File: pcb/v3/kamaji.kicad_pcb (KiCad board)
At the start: 2 copper layers, 100 x 100 mm, 41 parts, among them J1 UART, J10 USB_A, J2 ICSP, J3 RJ10, J4 RJ10, J5 RJ10, J6 RJ10, J7 RJ10, J8 RJ10, J9 USB_B, Q1 2N3904, Q2 IRL540N, SW1 SW_Push, SW2 SW_Push, SW3 SW_Push, U1 ATMEGA644P-20PU, U2 BOOST_24V, Y1 20MHz

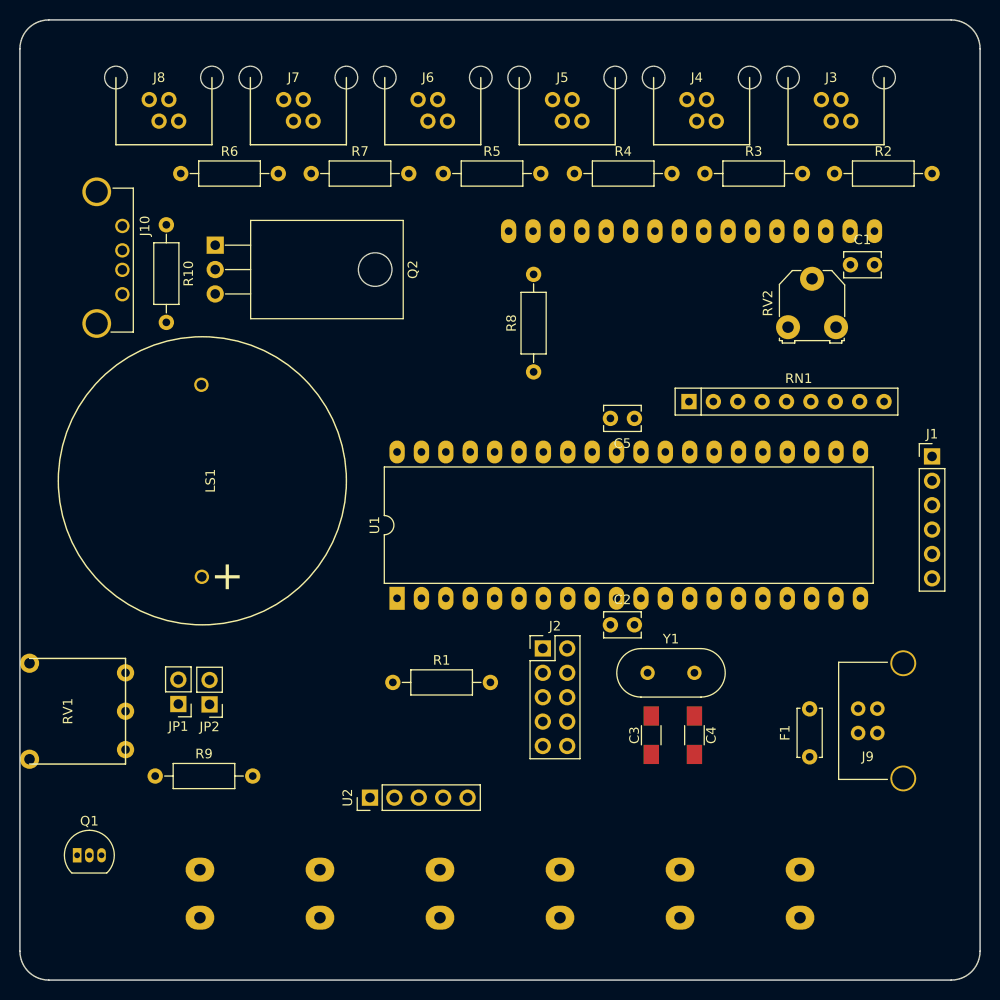
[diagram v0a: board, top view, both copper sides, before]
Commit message: mostly finish the v3 layout
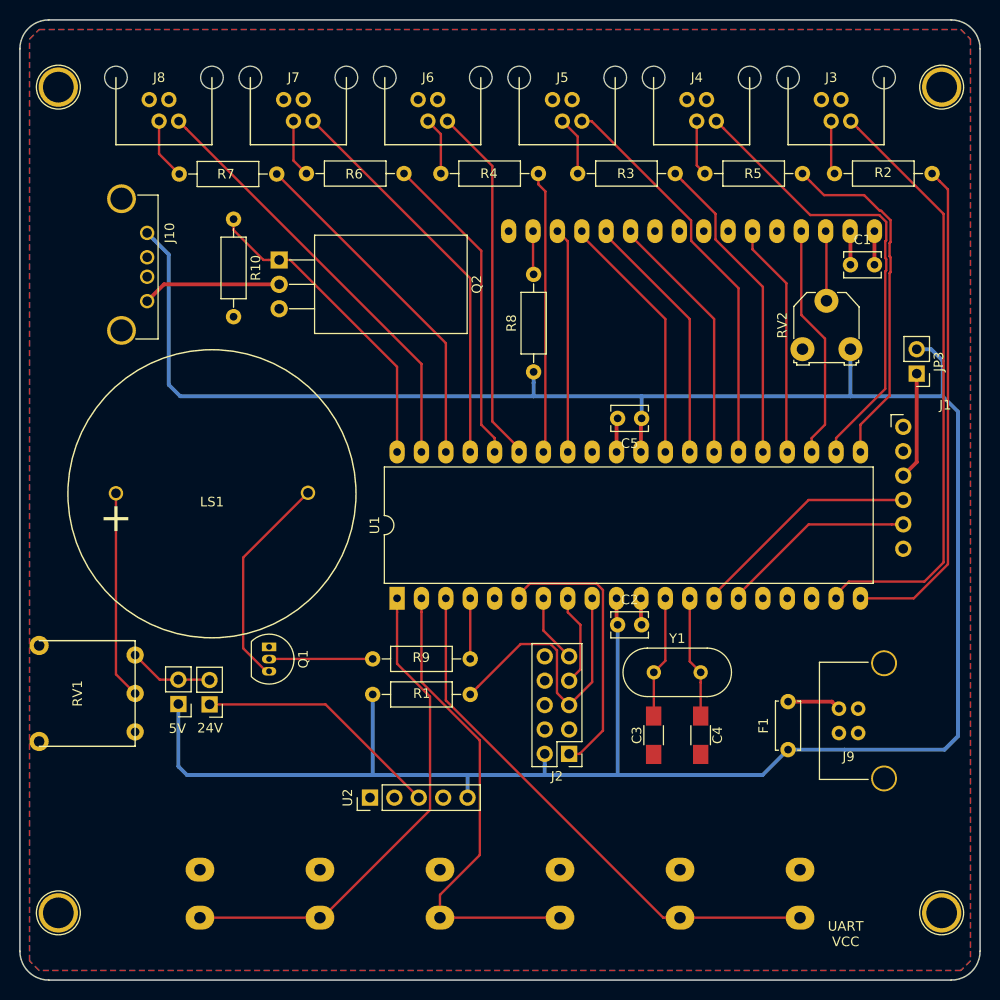
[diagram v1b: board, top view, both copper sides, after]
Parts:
- removed RN1: 10K, Resistors_THT:R_Array_SIP9
- added JP3: UART_PWR, Pin_Headers:Pin_Header_Straight_1x02_Pitch2.54mm, F.Cu at (143.4, 86.8)
- added REF**: 1pin, Connectors:1pin, F.Cu at (146.0, 143.0)
- added REF**: 1pin, Connectors:1pin, F.Cu at (54.0, 143.0)
- added REF**: 1pin, Connectors:1pin, F.Cu at (54.0, 57.0)
- added REF**: 1pin, Connectors:1pin, F.Cu at (146.0, 57.0)
- J1: value UART -> UART_6pin; footprint Pin_Headers:Pin_Header_Straight_1x06_Pitch2.54mm -> kamaji:Pin_Header_Angled_1x06_Pitch2.54mm
- Q2: footprint TO_SOT_Packages_THT:TO-220-3_Horizontal -> kamaji:TO-220-3_Horizontal
- moved Q1 29.5 mm to (76.0, 115.3), turned to 270 degrees
- moved R5 27.2 mm to (121.3, 66.0)
- moved R9 25.7 mm to (86.7, 116.5)
- moved R4 13.9 mm to (93.8, 66.0)
- moved R7 13.8 mm to (66.6, 66.0)
- moved R3 13.2 mm to (108.1, 66.0)
- moved R6 13.1 mm to (79.8, 66.0)
- moved J2 11.3 mm to (107.2, 126.4), turned to 180 degrees
- moved R10 7.02 mm to (72.2, 70.8)
- moved Q2 6.84 mm to (77.0, 75.0)
- moved J1 4.30 mm to (142.0, 92.4)
- moved RV2 2.74 mm to (131.5, 84.3)
- moved J10 2.68 mm to (63.2, 72.2)
- moved R1 2.44 mm to (86.7, 120.2)
- moved F1 2.37 mm to (130.0, 126.0)
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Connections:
- net /MC_RX renamed /AVR_RX
- net /MC_TX renamed /AVR_TX
- DS1 pad 11: Net-(DS1-Pad11) -> /LCD_D4
- DS1 pad 12: Net-(DS1-Pad12) -> /LCD_D5
- DS1 pad 13: Net-(DS1-Pad13) -> /LCD_D6
- DS1 pad 14: Net-(DS1-Pad14) -> /LCD_D7
- DS1 pad 4: Net-(DS1-Pad4) -> /LCD_RS
- DS1 pad 6: Net-(DS1-Pad6) -> /LCD_EN
- J1 pad 3: VCC -> Net-(J1-Pad3)
- J3 pad 2: /LED1 -> Net-(J3-Pad2)
- J4 pad 2: /LED2 -> Net-(J4-Pad2)
- J5 pad 2: /LED3 -> Net-(J5-Pad2)
- J6 pad 2: /LED4 -> Net-(J6-Pad2)
- J7 pad 2: /LED5 -> Net-(J7-Pad2)
- J8 pad 2: /LED6 -> Net-(J8-Pad2)
- R2 pad 1: /LED1 -> Net-(J3-Pad2)
- R2 pad 2: Net-(R2-Pad2) -> /LED1
- R3 pad 1: /LED2 -> Net-(J5-Pad2)
- R3 pad 2: Net-(R3-Pad2) -> /LED3
- R4 pad 1: /LED3 -> Net-(J6-Pad2)
- R4 pad 2: Net-(R4-Pad2) -> /LED4
- R5 pad 1: /LED4 -> Net-(J4-Pad2)
- R5 pad 2: Net-(R5-Pad2) -> /LED2
- R6 pad 1: /LED6 -> Net-(J7-Pad2)
- R6 pad 2: Net-(R6-Pad2) -> /LED5
- R7 pad 1: /LED5 -> Net-(J8-Pad2)
- R7 pad 2: Net-(R7-Pad2) -> /LED6
- U1 pad 1: /CBTN1 -> /CBTN3
- U1 pad 16: Net-(R2-Pad2) -> (no net)
- U1 pad 17: Net-(R3-Pad2) -> (no net)
- U1 pad 18: Net-(R4-Pad2) -> (no net)
- U1 pad 19: Net-(R5-Pad2) -> /BTN1
- U1 pad 20: /LAMP -> /LED1
- U1 pad 21: /SOUND -> /LED2
- U1 pad 22: /BTN1 -> /BTN2
- U1 pad 23: /BTN2 -> /LCD_RS
- U1 pad 24: /BTN3 -> /LCD_EN
- U1 pad 25: /BTN4 -> /LED3
- U1 pad 26: /BTN5 -> /BTN3
- U1 pad 27: /BTN6 -> /LCD_D4
- U1 pad 28: (no net) -> /LCD_D5
- U1 pad 29: (no net) -> /LCD_D6
- U1 pad 3: /CBTN3 -> /CBTN1
- U1 pad 33: Net-(R7-Pad2) -> /LCD_D7
- U1 pad 34: Net-(R6-Pad2) -> /LED4
- U1 pad 35: Net-(DS1-Pad14) -> /BTN4
- U1 pad 36: Net-(DS1-Pad13) -> /LED5
- U1 pad 37: Net-(DS1-Pad12) -> /BTN5
- U1 pad 38: Net-(DS1-Pad11) -> /LED6
- U1 pad 39: Net-(DS1-Pad4) -> /BTN6
- U1 pad 4: (no net) -> /SOUND
- U1 pad 40: Net-(DS1-Pad6) -> /LAMP
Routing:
- net VCC: track 0.00 -> 279.2 mm
- net /BTN1: track 0.00 -> 62.9 mm
- net /CBTN1: track 0.00 -> 56.9 mm
- net /CBTN3: track 0.00 -> 52.1 mm
- net /LED1: track 0.00 -> 52.0 mm
- net /CBTN2: track 0.00 -> 50.0 mm
- net /BTN2: track 0.00 -> 48.2 mm
- net /BTN6: track 0.00 -> 44.9 mm
- net /BTN3: track 0.00 -> 42.2 mm
- net /BTN5: track 0.00 -> 41.2 mm
- net /BTN4: track 0.00 -> 37.5 mm
- net /LED2: track 0.00 -> 36.7 mm
- net /LED6: track 0.00 -> 36.2 mm
- net /LED3: track 0.00 -> 33.2 mm
- net /LAMP: track 0.00 -> 32.9 mm
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- added copper zone on B.Cu, net GND
- added copper zone on F.Cu, net GND
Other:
- net class Power added: clearance 0.3, trace_width 0.4, via_dia 0.6, via_drill 0.4
- board text added: "24V"
- board text added: "5V"
- board text added: "UART VCC"

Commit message: v3 PCB: final touches
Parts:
- C3, C4: footprint Capacitors_SMD:C_1206_HandSoldering -> Capacitors_THT:C_Disc_D3.8mm_W2.6mm_P2.50mm
- moved C4 2.50 mm to (120.9, 122.0)
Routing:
- net Net-(C4-Pad1): track 12.7 -> 12.2 mm
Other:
- board text added: "Kamaji v3"
- board text added: "github.com/iley/kamaji"

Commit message: minor pcb changes
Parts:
- moved Q1 2.48 mm to (77.5, 117.2)
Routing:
- net Net-(Q1-Pad2): track 10.8 -> 10.0 mm
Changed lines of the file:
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@@
   )
   (module TO_SOT_Packages_THT:TO-92_Inline_Narrow_Oval (layer F.Cu)
-    (at 75.95 115.3 270)
+    (at 77.5 117.23 270)
     (descr "TO-92 leads in-line, narrow, oval pads, drill 0.6mm (see NXP sot054_po.pdf)")
     (tags "to-92 sc-43 sc-43a sot54 PA33 transistor")
@@
     (descr "Through hole straight pin header, 1x02, 2.54mm pitch, single row")
     (tags "Through hole pin header THT 1x02 2.54mm single row")
-    (fp_text reference JP3 (at -2.3 1.24 270) (layer F.SilkS)
+    (fp_text reference JP3 (at -2.3 1.24 270) (layer F.SilkS) hide
       (effects (font (size 1 1) (thickness 0.15)))
     )
@@
     (effects (font (size 1 1) (thickness 0.15)))
   )
-  (gr_text "UART\nVCC" (at 136 145.2) (layer F.SilkS)
+  (gr_text "UART\nVCC" (at 143.5 81) (layer F.SilkS)
     (effects (font (size 1 1) (thickness 0.2)))
   )
@@
   (segment (start 62 116.15) (end 64.56 118.71) (width 0.25) (layer F.Cu) (net 25))
   (segment (start 64.56 118.71) (end 66.5 118.71) (width 0.25) (layer F.Cu) (net 25))
-  (segment (start 69.75 121.29) (end 81.83 121.29) (width 0.25) (layer F.Cu) (net 26))
-  (segment (start 81.83 121.29) (end 91.54 131) (width 0.25) (layer F.Cu) (net 26))
-  (segment (start 80 99.25) (end 73.25 106) (width 0.25) (layer F.Cu) (net 27))
-  (segment (start 73.25 115.44) (end 75.65 117.84) (width 0.25) (layer F.Cu) (net 27))
-  (segment (start 73.25 106) (end 73.25 115.44) (width 0.25) (layer F.Cu) (net 27))
-  (segment (start 75.65 117.84) (end 75.95 117.84) (width 0.25) (layer F.Cu) (net 27))
+  (segment (start 91.54 131) (end 81.83 121.29) (width 0.25) (layer F.Cu) (net 26))
+  (segment (start 81.83 121.29) (end 69.75 121.29) (width 0.25) (layer F.Cu) (net 26))
+  (segment (start 80 99.25) (end 76.324999 102.925001) (width 0.25) (layer F.Cu) (net 27))
+  (segment (start 76.324999 102.925001) (end 76.324999 118.894999) (width 0.25) (layer F.Cu) (net 27))
+  (segment (start 76.324999 118.894999) (end 77.2 119.77) (width 0.25) (layer F.Cu) (net 27))
+  (segment (start 77.2 119.77) (end 77.5 119.77) (width 0.25) (layer F.Cu) (net 27))
   (segment (start 60 99.3) (end 60 118.15) (width 0.25) (layer F.Cu) (net 28))
   (segment (start 60 118.15) (end 62 120.15) (width 0.25) (layer F.Cu) (net 28))
-  (segment (start 86.74 116.55) (end 75.97 116.55) (width 0.25) (layer F.Cu) (net 29))
-  (segment (start 75.97 116.55) (end 75.95 116.57) (width 0.25) (layer F.Cu) (net 29))
+  (segment (start 77.5 118.5) (end 84.79 118.5) (width 0.25) (layer F.Cu) (net 29))
+  (segment (start 84.79 118.5) (end 86.74 116.55) (width 0.25) (layer F.Cu) (net 29))
   (segment (start 72.25 70.75) (end 72.25 71.88137) (width 0.25) (layer F.Cu) (net 30))
   (segment (start 72.25 71.88137) (end 75.36863 75) (width 0.25) (layer F.Cu) (net 30))
